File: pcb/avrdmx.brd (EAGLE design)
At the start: 53 x 60.9 mm, 15 parts, among them IC1 75176AP, IC2 75176AP, IC3 75176AP, IC4 75176AP, IC5 7404N, U1 ARDUINO_SHIELDLABEL

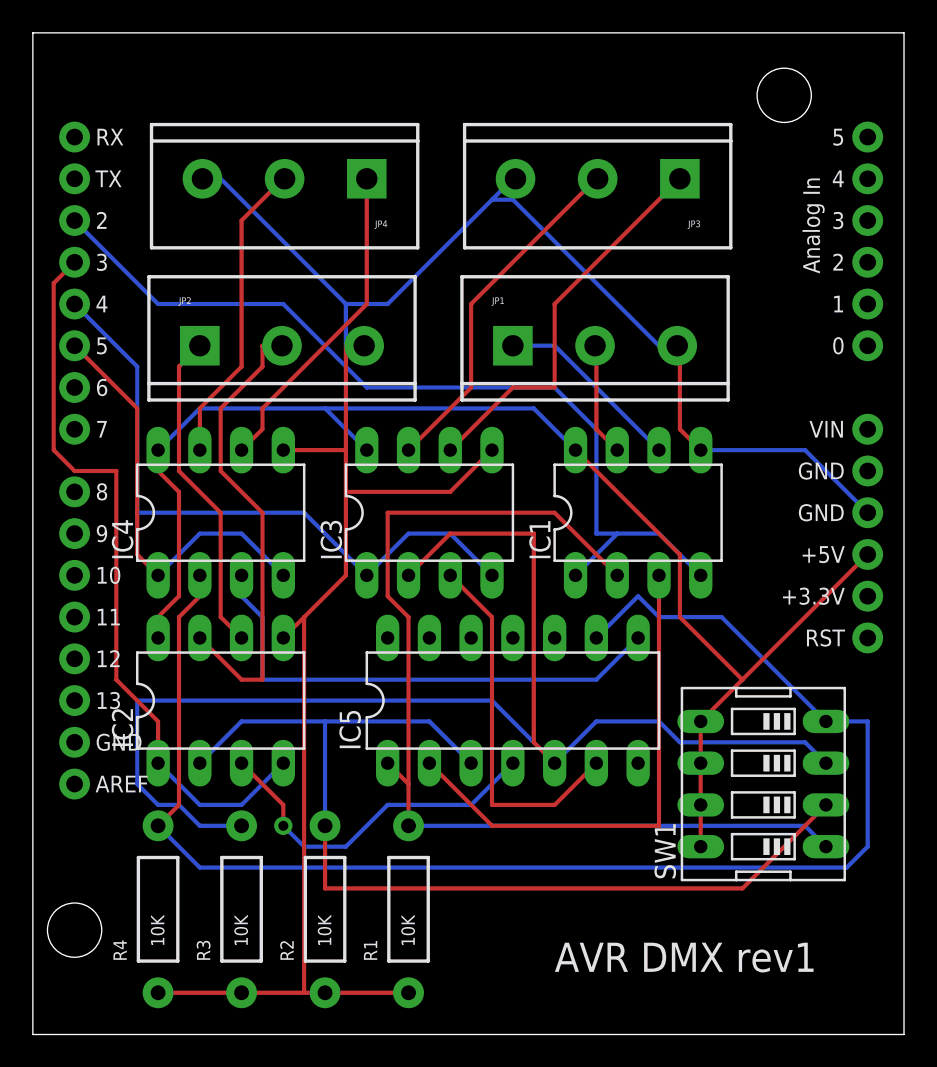
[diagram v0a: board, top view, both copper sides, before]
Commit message: switched from arduino pins 2-5 to 8-11
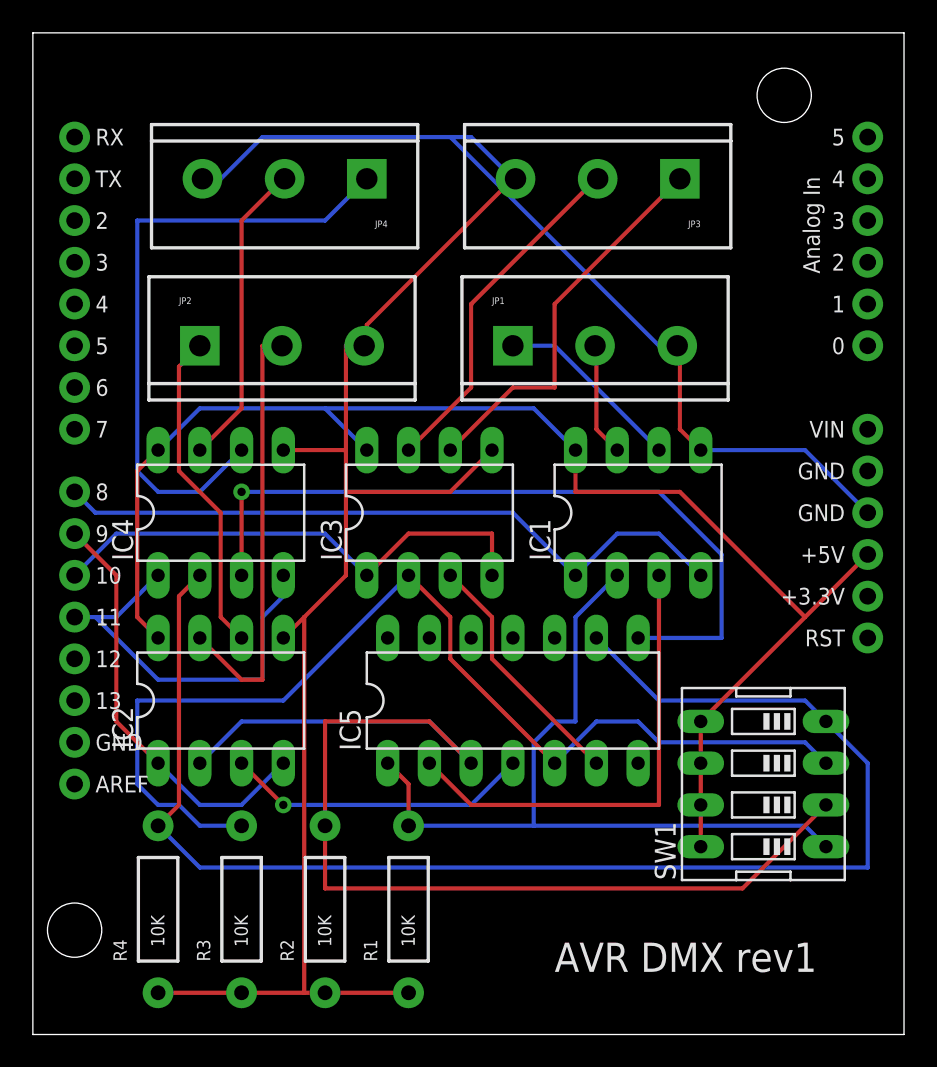
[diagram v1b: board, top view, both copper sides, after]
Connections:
- net N$1: now also U1.D8; no longer U1.D2
- net N$2: now also U1.D9; no longer U1.D3
- net N$3: now also U1.D10; no longer U1.D4
- net N$4: now also U1.D11; no longer U1.D5
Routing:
- net N$2: track 44.8 -> 25.8 mm
- net N$21: track 19.7 -> 38.2 mm
- net N$13: track 81.2 -> 65.9 mm
- net N$5: track 30.8 -> 46.0 mm, vias 0 -> 1
- net N$11: track 62.8 -> 48.4 mm
- net N$1: track 54.4 -> 42.3 mm
- net N$6: track 135.1 -> 145.5 mm
- net N$12: track 61.4 -> 71.3 mm
- net N$3: track 39.6 -> 31.1 mm
- net N$7: track 22.4 -> 15.1 mm
- net N$8: track 21.5 -> 18.6 mm
- net N$14: track 89.4 -> 86.5 mm
- net N$18: track 28.5 -> 26.4 mm
- net N$9: track 30.8 -> 29.0 mm
- net N$15: track 83.7 -> 85.2 mm
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
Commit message: board rev3 - fix 7404N Vcc and GND
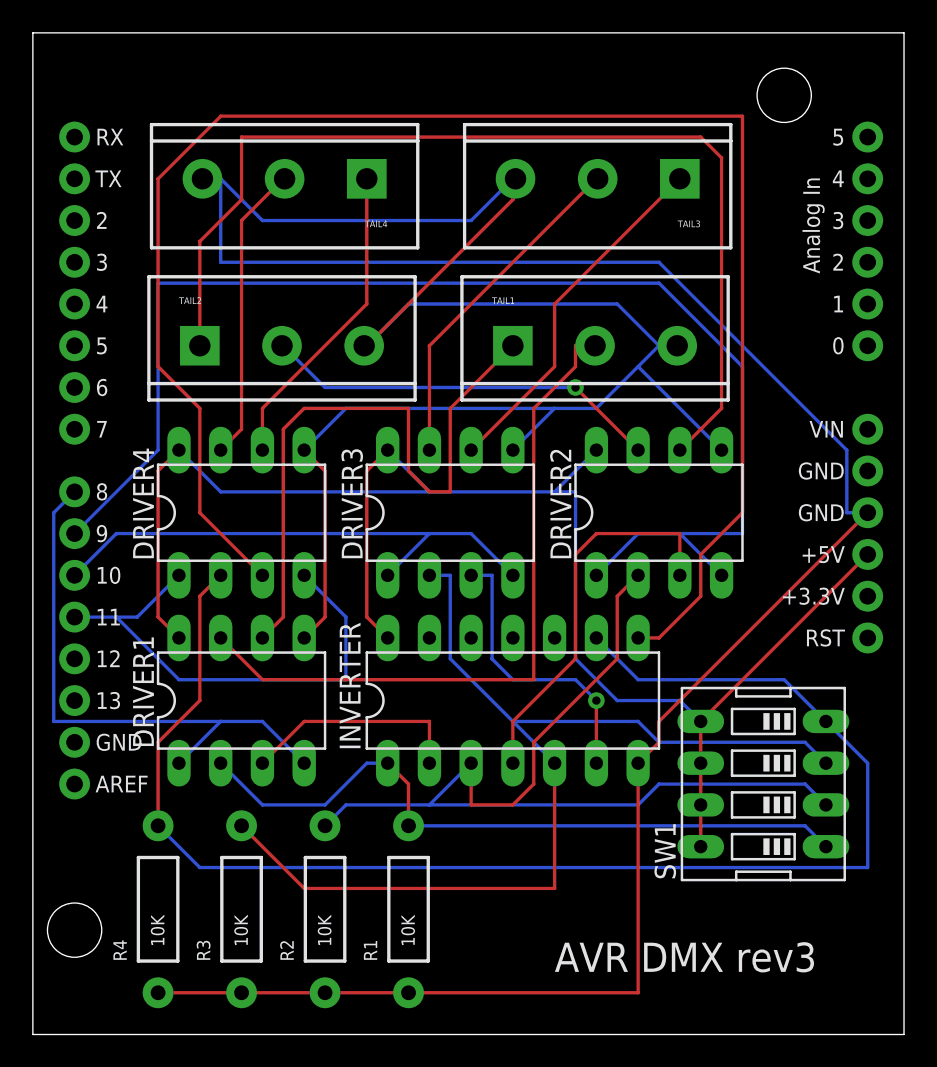
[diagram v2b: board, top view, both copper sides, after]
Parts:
- removed IC1, IC2, IC3, IC4: 75176AP, 751xx:DIL08
- added DRIVER1, DRIVER2, DRIVER3, DRIVER4: 75176AP, 751xx:DIL08
- renumbered IC5 to INVERTER, JP1 to TAIL1, JP2 to TAIL2, JP3 to TAIL3, JP4 to TAIL4
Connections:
- removed net N$15: IC1.8, IC2.8, IC3.8, IC4.8, SW1.5, SW1.6, SW1.7, SW1.8, U1.5V
- removed net N$6: IC1.5, IC2.5, IC3.5, IC4.5, R1.P$1, R2.P$1, R3.P$1, R4.P$1, TAIL1.3, TAIL2.3, TAIL3.3, TAIL4.3, U1.GND@0
- net GND: now also DRIVER1.5, DRIVER2.5, DRIVER3.5, DRIVER4.5, R1.P$1, R2.P$1, R3.P$1, R4.P$1, TAIL1.3, TAIL2.3, TAIL3.3, TAIL4.3, U1.GND@0
- net N$1: now also DRIVER1.1, DRIVER1.4; no longer IC1.1, IC1.4
- net N$10: now also DRIVER1.6; no longer IC1.6
- net N$11: now also DRIVER1.2; no longer IC1.2
- net N$12: now also DRIVER2.2; no longer IC2.2
- net N$13: now also DRIVER3.2; no longer IC3.2
- net N$14: now also DRIVER4.2; no longer IC4.2
- net N$16: now also DRIVER1.7; no longer IC1.7
- net N$17: now also DRIVER2.6; no longer IC2.6
- net N$18: now also DRIVER2.7; no longer IC2.7
- net N$19: now also DRIVER3.6; no longer IC3.6
- net N$2: now also DRIVER2.1, DRIVER2.4; no longer IC2.1, IC2.4
- net N$20: now also DRIVER3.7; no longer IC3.7
- net N$21: now also DRIVER4.6; no longer IC4.6
- net N$22: now also DRIVER4.7; no longer IC4.7
- net N$3: now also DRIVER3.1, DRIVER3.4; no longer IC3.1, IC3.4
- net N$4: now also DRIVER4.1, DRIVER4.4; no longer IC4.1, IC4.4
- net N$5: now also DRIVER4.3; no longer IC4.3
- net N$7: now also DRIVER3.3; no longer IC3.3
- net N$8: now also DRIVER2.3; no longer IC2.3
- net N$9: now also DRIVER1.3; no longer IC1.3
- net VCC: now also DRIVER1.8, DRIVER2.8, DRIVER3.8, DRIVER4.8, SW1.5, SW1.6, SW1.7, SW1.8, U1.5V
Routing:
- net GND: track 0.00 -> 221.2 mm
- net N$6: track 145.5 -> 0.00 mm
- net VCC: track 0.00 -> 98.7 mm
- net N$15: track 85.2 -> 0.00 mm
- net N$5: track 46.0 -> 99.0 mm, vias 1 -> 0
- net N$2: track 25.8 -> 78.7 mm
- net N$17: track 19.9 -> 62.3 mm
- net N$16: track 6.96 -> 42.7 mm
- net N$10: track 11.5 -> 38.7 mm
- net N$21: track 38.2 -> 19.1 mm
- net N$9: track 29.0 -> 13.8 mm
- net N$12: track 71.3 -> 57.9 mm
- net N$1: track 42.3 -> 34.4 mm
- net N$11: track 48.4 -> 42.5 mm
- net N$4: track 24.7 -> 30.4 mm
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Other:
- board text added: "AVR DMX rev3"
- board text removed: "AVR DMX rev1"

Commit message: schematic changes from a long time ago, not sure if they're good
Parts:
- removed INVERTER: 7404N, 74xx-us:DIL14
- removed R1, R2, R3, R4: 10K, SparkFun-Resistors:AXIAL-0.4
- removed SW1: (no value), special:EDG-04
- removed TAIL1, TAIL2, TAIL3, TAIL4: (no value), SparkFun-Connectors:SCREWTERMINAL-5MM-3
- added DRIVER5: 75176AP, 751xx:DIL08
- added IR1: IR IN, pinhead:1X03
- added OUT1, OUT2, OUT3, OUT4: NC5FAV, avrdmx:NC5FAV
- added TAIL5: DMX IN, SparkFun-Connectors:SCREWTERMINAL-5MM-3
- moved DRIVER1 36.6 mm to (47.0, 27.9)
- moved DRIVER4 21.0 mm to (31.8, 43.2)
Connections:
- removed net N$17: DRIVER2.6, TAIL2.1
- removed net N$18: DRIVER2.7, TAIL2.2
- removed net N$19: DRIVER3.6, TAIL3.1
- removed net N$20: DRIVER3.7, TAIL3.2
- removed net N$21: DRIVER4.6, TAIL4.1
- removed net N$22: DRIVER4.7, TAIL4.2
- new net N$15: DRIVER4.6, OUT4.3
- new net N$6: DRIVER5.6, TAIL5.1
- net GND: now also DRIVER1.1, DRIVER2.1, DRIVER3.1, DRIVER4.1, DRIVER5.2, DRIVER5.3, DRIVER5.4, DRIVER5.5, IR1.2, OUT1.1, OUT2.1, OUT3.1, OUT4.1, TAIL5.3; no longer INVERTER.7, R1.P$1, R2.P$1, R3.P$1, R4.P$1, TAIL1.3, TAIL2.3, TAIL3.3, TAIL4.3
- net N$1: no longer DRIVER1.1
- net N$10: now also OUT1.3; no longer TAIL1.1
- net N$11: now also DRIVER2.7, OUT2.2; no longer DRIVER1.2, INVERTER.1, R1.P$2, SW1.1
- net N$12: now also DRIVER2.6, OUT2.3; no longer DRIVER2.2, INVERTER.3, R2.P$2, SW1.2
- net N$13: now also DRIVER3.7, OUT3.2; no longer DRIVER3.2, INVERTER.5, R3.P$2, SW1.3
- net N$14: now also DRIVER3.6, OUT3.3; no longer DRIVER4.2, INVERTER.9, R4.P$2, SW1.4
- net N$16: now also DRIVER4.7, OUT4.2; no longer DRIVER1.7, TAIL1.2
- net N$2: no longer DRIVER2.1
- net N$3: no longer DRIVER3.1
- net N$4: no longer DRIVER4.1
- net N$5: now also IR1.1, U1.D7; no longer DRIVER4.3, INVERTER.8
- net N$7: now also DRIVER5.7, TAIL5.2; no longer DRIVER3.3, INVERTER.6
- net N$8: now also DRIVER1.7, OUT1.2; no longer DRIVER2.3, INVERTER.4
- net N$9: now also DRIVER5.1, U1.RX; no longer DRIVER1.3, INVERTER.2
- net VCC: now also DRIVER1.2, DRIVER1.3, DRIVER2.2, DRIVER2.3, DRIVER3.2, DRIVER3.3, DRIVER4.2, DRIVER4.3, DRIVER5.8, IR1.3; no longer INVERTER.14, SW1.5, SW1.6, SW1.7, SW1.8
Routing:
- net GND: track 221.2 -> 107.9 mm
- net N$5: track 99.0 -> 0.00 mm
- net VCC: track 98.7 -> 0.00 mm
- net N$14: track 87.1 -> 0.00 mm
- net N$13: track 63.7 -> 0.00 mm
- net N$17: track 62.3 -> 0.00 mm
- net N$12: track 57.9 -> 0.00 mm
- net N$16: track 42.7 -> 0.00 mm
- net N$11: track 42.5 -> 0.00 mm
- net N$10: track 38.7 -> 0.00 mm
- net N$18: track 24.3 -> 0.00 mm, vias 1 -> 0
- net N$8: track 23.7 -> 0.00 mm
- net N$19: track 21.8 -> 0.00 mm
- net N$20: track 20.8 -> 0.00 mm
- net N$21: track 19.1 -> 0.00 mm
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
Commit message: finish PCB rev3
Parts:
- removed OUT1, OUT2, OUT3, OUT4: NC5FAV, avrdmx:NC5FAV
- removed TAIL5: DMX IN, SparkFun-Connectors:SCREWTERMINAL-5MM-3
- added U$1, U$2, U$3, U$4, U$5: B3P-VH, avrdmx:B3P-VH
- moved DRIVER1 27.9 mm to (35.6, 53.3), turned to 180 degrees
- moved DRIVER2 22.9 mm to (15.2, 53.3), turned to 180 degrees
- moved DRIVER4 16.6 mm to (15.2, 41.9), turned to 180 degrees
- moved DRIVER3 14.4 mm to (35.6, 41.9), turned to 180 degrees
- moved DRIVER5 13.7 mm to (15.2, 30.5), turned to 180 degrees
- moved IR1 4.02 mm to (48.3, 34.3), turned to 90 degrees
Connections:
- net GND: now also U$1.G, U$2.G, U$3.G, U$4.G, U$5.A; no longer OUT1.1, OUT2.1, OUT3.1, OUT4.1, TAIL5.3
- net N$10: now also U$1.A; no longer OUT1.3
- net N$11: now also U$2.B; no longer OUT2.2
- net N$12: now also U$2.A; no longer OUT2.3
- net N$13: now also U$3.B; no longer OUT3.2
- net N$14: now also U$3.A; no longer OUT3.3
- net N$15: now also U$4.A; no longer OUT4.3
- net N$16: now also U$4.B; no longer OUT4.2
- net N$5: now also U1.A0; no longer U1.D7
- net N$6: now also U$5.G; no longer TAIL5.1
- net N$7: now also U$5.B; no longer TAIL5.2
- net N$8: now also U$1.B; no longer OUT1.2
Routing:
- net GND: track 107.9 -> 224.2 mm
- net VCC: track 0.00 -> 110.3 mm
- net N$9: track 0.00 -> 70.8 mm
- net N$12: track 0.00 -> 52.5 mm, vias 0 -> 1
- net N$16: track 0.00 -> 46.9 mm
- net N$8: track 0.00 -> 42.7 mm
- net N$13: track 0.00 -> 35.5 mm
- net N$5: track 0.00 -> 32.6 mm
- net N$4: track 40.9 -> 8.89 mm
- net N$14: track 0.00 -> 30.5 mm
- net N$11: track 0.00 -> 27.8 mm, vias 0 -> 2
- net N$15: track 0.00 -> 27.4 mm
- net N$7: track 0.00 -> 25.2 mm
- net N$10: track 0.00 -> 18.5 mm
- net N$6: track 0.00 -> 17.9 mm
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
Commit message: PCB rev4 - fixes:  - larger holes for DMX cable headers  - fix receiver driver wiring  - better labels
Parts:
- ANALOG_IN: value IR IN -> ANALOG IN
- renumbered DRIVER5 to DRIVER_IN, IR1 to ANALOG_IN, U$1 to DMX1, U$2 to DMX2, U$3 to DMX3, U$4 to DMX4, U$5 to DMX_IN
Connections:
- removed net N$6: DMX_IN.G, DRIVER_IN.6
- new net N$17: DMX_IN.A, DRIVER_IN.6
- net GND: now also DMX_IN.G; no longer DMX_IN.A
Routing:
- net N$2: track 55.8 -> 11.5 mm
- net GND: track 224.2 -> 188.6 mm
- net N$17: track 0.00 -> 33.5 mm
- net N$12: track 52.5 -> 24.2 mm, vias 1 -> 0
- net N$1: track 39.0 -> 67.0 mm, vias 1 -> 0
- net N$8: track 42.7 -> 23.5 mm
- net N$6: track 17.9 -> 0.00 mm
- net N$16: track 46.9 -> 31.3 mm
- net VCC: track 110.3 -> 106.3 mm
- net N$11: track 27.8 -> 30.7 mm, vias 2 -> 0
- net N$13: track 35.5 -> 37.0 mm
- net N$14: track 30.5 -> 32.0 mm, vias 0 -> 1
- net N$10: track 18.5 -> 17.0 mm
- net N$15: track 27.4 -> 26.3 mm
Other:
- board text added: "AVR DMX rev4"
- board text removed: "AVR DMX rev3"
